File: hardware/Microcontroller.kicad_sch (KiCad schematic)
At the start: 1 part

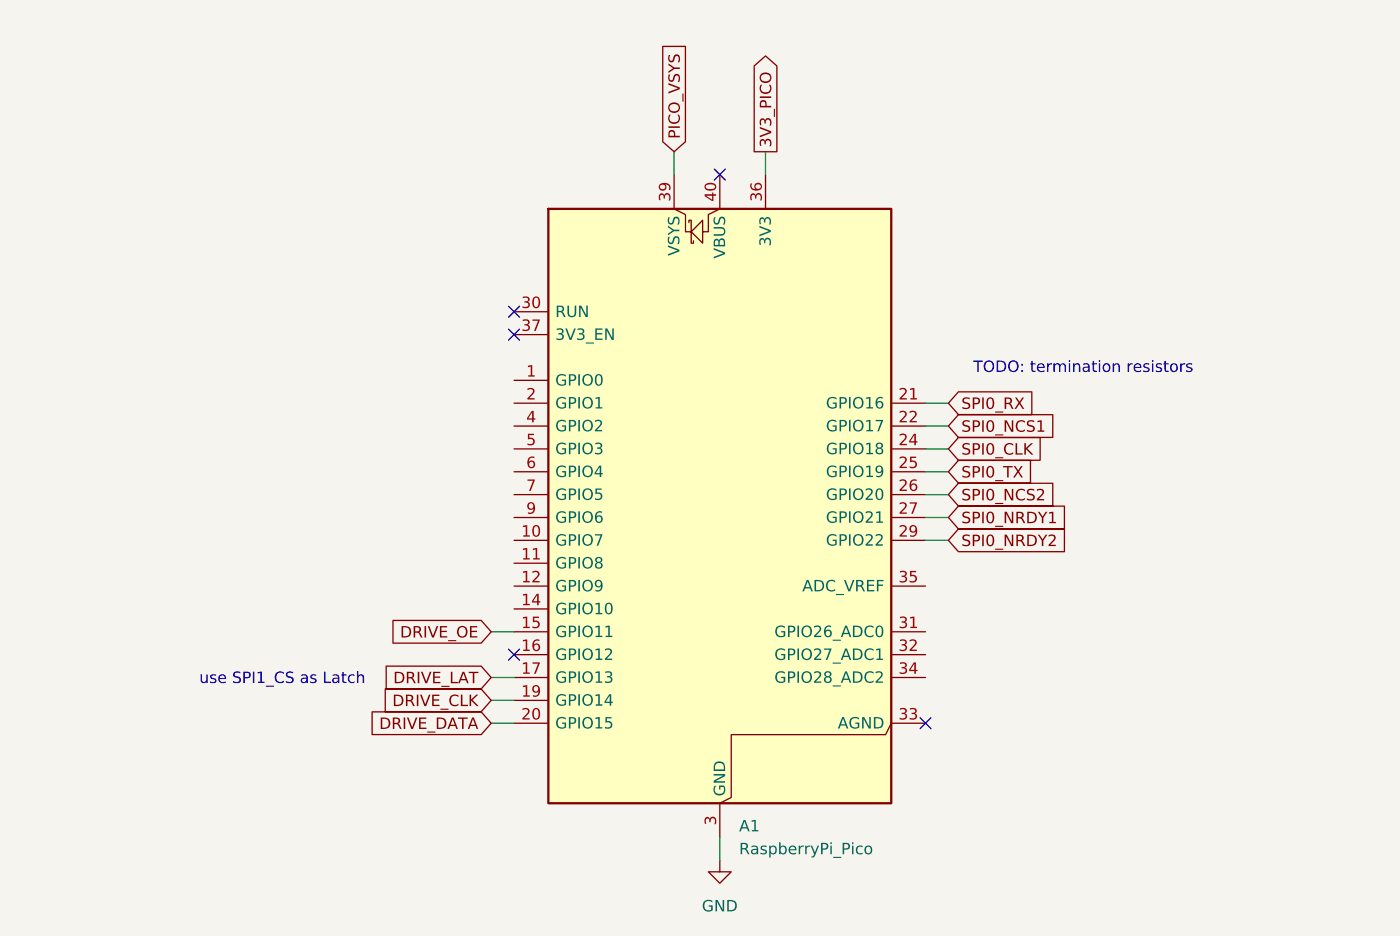
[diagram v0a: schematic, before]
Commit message: updated Power input on schematic
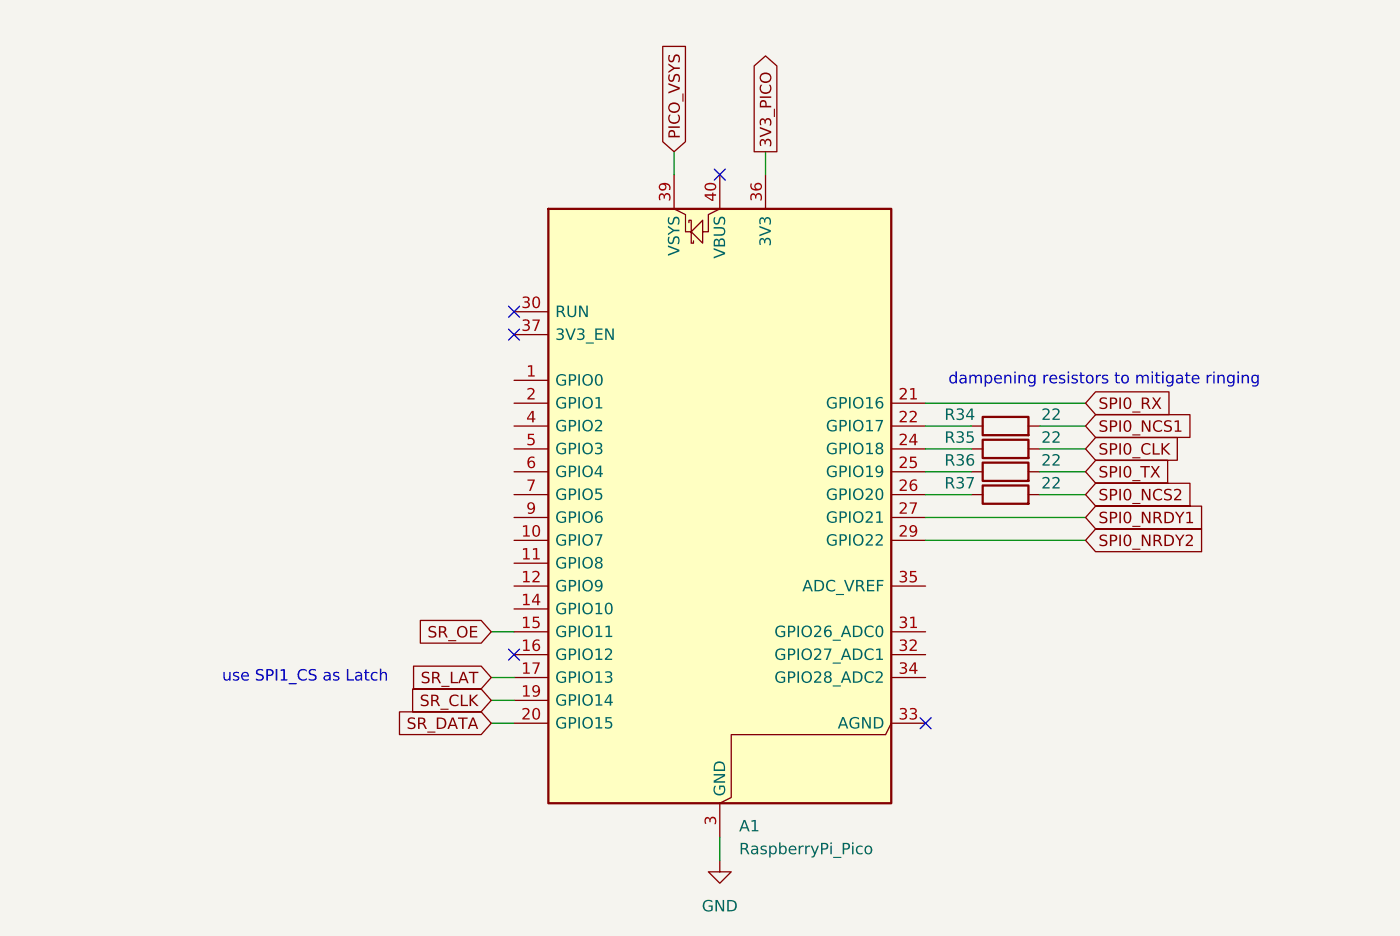
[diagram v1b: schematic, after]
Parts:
- added R34, R35, R36, R37: 22, symbol Device:R
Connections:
- net SPI0_CLK: now also R35.2; no longer A1.24 (GPIO18)
- net SPI0_NCS1: now also R34.2; no longer A1.22 (GPIO17)
- net SPI0_NCS2: now also R37.2; no longer A1.26 (GPIO20)
- net SPI0_TX: now also R36.2; no longer A1.25 (GPIO19)
- net DRIVE_CLK renamed SR_CLK
- net DRIVE_DATA renamed SR_DATA
- net DRIVE_LAT renamed SR_LAT
- net DRIVE_OE renamed SR_OE
- new net: A1.25 (GPIO19), R36.1
- new net: A1.24 (GPIO18), R35.1
- new net: A1.26 (GPIO20), R37.1
- new net: A1.22 (GPIO17), R34.1
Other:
- note added: "dampening resistors to mitigate ringing"
- note removed: "TODO: termination resistors"

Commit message: reworked power protection circuit and fixed ERC errors
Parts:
- R3: renamed from R34; footprint (none) -> Resistor_SMD:R_0603_1608Metric
- R4: renamed from R35; footprint (none) -> Resistor_SMD:R_0603_1608Metric
- R5: renamed from R36; footprint (none) -> Resistor_SMD:R_0603_1608Metric
- R6: renamed from R37; footprint (none) -> Resistor_SMD:R_0603_1608Metric
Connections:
- net LED_DI: now reaches A1.9 (GPIO6)
- no-connect marks 5 -> 19
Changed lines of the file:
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@@
+	)
+	(no_connect
+		(at 124.46 111.76)
+	)
+	(no_connect
+		(at 170.18 114.3)
 	)
 	(no_connect
@@
 	)
 	(no_connect
+		(at 170.18 119.38)
+	)
+	(no_connect
+		(at 124.46 109.22)
+	)
+	(no_connect
+		(at 124.46 96.52)
+	)
+	(no_connect
+		(at 124.46 116.84)
+	)
+	(no_connect
+		(at 124.46 93.98)
+	)
+	(no_connect
+		(at 124.46 99.06)
+	)
+	(no_connect
+		(at 170.18 124.46)
+	)
+	(no_connect
 		(at 170.18 129.54)
 	)
 	(no_connect
+		(at 124.46 91.44)
+	)
+	(no_connect
 		(at 124.46 121.92)
 	)
 	(no_connect
+		(at 124.46 101.6)
+	)
+	(no_connect
+		(at 124.46 114.3)
+	)
+	(no_connect
+		(at 170.18 121.92)
+	)
+	(no_connect
+		(at 124.46 104.14)
+	)
+	(no_connect
 		(at 124.46 86.36)
 	)
@@
 	(wire
 		(pts
+			(xy 152.4 66.04) (xy 152.4 68.58)
+		)
+		(stroke
+			(width 0)
+			(type default)
+		)
+	)
+	(wire
+		(pts
+			(xy 170.18 96.52) (xy 175.26 96.52)
+		)
+		(stroke
+			(width 0)
+			(type default)
+		)
+	)
+	(wire
+		(pts
+			(xy 121.92 124.46) (xy 124.46 124.46)
+		)
+		(stroke
+			(width 0)
+			(type default)
+		)
+	)
+	(wire
+		(pts
+			(xy 121.92 129.54) (xy 124.46 129.54)
+		)
+		(stroke
+			(width 0)
+			(type default)
+		)
+	)
+	(wire
+		(pts
+			(xy 182.88 96.52) (xy 187.96 96.52)
+		)
+		(stroke
+			(width 0)
+			(type default)
+		)
+	)
+	(wire
+		(pts
+			(xy 121.92 127) (xy 124.46 127)
+		)
+		(stroke
+			(width 0)
+			(type default)
+		)
+	)
+	(wire
+		(pts
+			(xy 170.18 106.68) (xy 187.96 106.68)
+		)
+		(stroke
+			(width 0)
+			(type default)
+		)
+	)
+	(wire
+		(pts
 			(xy 142.24 66.04) (xy 142.24 68.58)
 		)
@@
 	(wire
 		(pts
-			(xy 152.4 66.04) (xy 152.4 68.58)
-		)
-		(stroke
-			(width 0)
-			(type default)
-		)
-	)
-	(wire
-		(pts
-			(xy 170.18 96.52) (xy 175.26 96.52)
-		)
-		(stroke
-			(width 0)
-			(type default)
-		)
-	)
-	(wire
-		(pts
-			(xy 121.92 124.46) (xy 124.46 124.46)
-		)
-		(stroke
-			(width 0)
-			(type default)
-		)
-	)
-	(wire
-		(pts
-			(xy 121.92 129.54) (xy 124.46 129.54)
-		)
-		(stroke
-			(width 0)
-			(type default)
-		)
-	)
-	(wire
-		(pts
-			(xy 182.88 96.52) (xy 187.96 96.52)
-		)
-		(stroke
-			(width 0)
-			(type default)
-		)
-	)
-	(wire
-		(pts
-			(xy 121.92 127) (xy 124.46 127)
-		)
-		(stroke
-			(width 0)
-			(type default)
-		)
-	)
-	(wire
-		(pts
-			(xy 170.18 106.68) (xy 187.96 106.68)
+			(xy 121.92 106.68) (xy 124.46 106.68)
 		)
 		(stroke
@@
 		)
 	)
+	(global_label "LED_DI"
+		(shape input)
+		(at 121.92 106.68 180)
+		(fields_autoplaced yes)
+		(effects
+			(font
+				(size 1.27 1.27)
+			)
+			(justify right)
+		)
+		(property "Intersheetrefs" "${INTERSHEET_REFS}"
+			(at 112.6453 106.68 0)
+			(hide yes)
+			(show_name no)
+			(do_not_autoplace no)
+			(effects
+				(font
+					(size 1.27 1.27)
+				)
+				(justify right)
+			)
+		)
+	)
 	(global_label "SPI0_NRDY2"
 		(shape input)
@@
 		)
 	)
+	(global_label "PICO_VSYS"
+		(shape input)
+		(at 142.24 66.04 90)
+		(fields_autoplaced yes)
+		(effects
+			(font
+				(size 1.27 1.27)
+			)
+			(justify left)
+		)
+		(property "Intersheetrefs" "${INTERSHEET_REFS}"
+			(at 142.24 53.0157 90)
+			(hide yes)
+			(show_name no)
+			(do_not_autoplace no)
+			(effects
+				(font
+					(size 1.27 1.27)
+				)
+				(justify left)
+			)
+		)
+	)
 	(global_label "SR_DATA"
 		(shape input)
@@
 		)
 	)
-	(global_label "PICO_VSYS"
-		(shape input)
-		(at 142.24 66.04 90)
-		(fields_autoplaced yes)
-		(effects
-			(font
-				(size 1.27 1.27)
-			)
-			(justify left)
-		)
-		(property "Intersheetrefs" "${INTERSHEET_REFS}"
-			(at 142.24 53.0157 90)
-			(hide yes)
-			(show_name no)
-			(do_not_autoplace no)
-			(effects
-				(font
-					(size 1.27 1.27)
-				)
-				(justify left)
-			)
-		)
-	)
 	(global_label "3V3_PICO"
-		(shape output)
+		(shape input)
 		(at 152.4 66.04 90)
 		(fields_autoplaced yes)
@@
 		(in_pos_files yes)
 		(dnp no)
-		(property "Reference" "R36"
+		(property "Reference" "R5"
 			(at 173.99 100.33 90)
 			(show_name no)
@@
 			)
 		)
-		(property "Footprint" ""
+		(property "Footprint" "Resistor_SMD:R_0603_1608Metric"
 			(at 179.07 103.378 90)
 			(hide yes)
@@
 			(project "ExpressionController"
 				(path "/acb9d00b-1122-4203-9813-1d558ab77d86/6aaa6853-9d8e-4732-9d59-0d7219d4a5ec"
-					(reference "R36")
+					(reference "R5")
 					(unit 1)
 				)
@@
 		(in_pos_files yes)
 		(dnp no)
-		(property "Reference" "R35"
+		(property "Reference" "R4"
 			(at 173.99 97.79 90)
 			(show_name no)
@@
 			)
 		)
-		(property "Footprint" ""
+		(property "Footprint" "Resistor_SMD:R_0603_1608Metric"
 			(at 179.07 100.838 90)
 			(hide yes)
@@
 			(project "ExpressionController"
 				(path "/acb9d00b-1122-4203-9813-1d558ab77d86/6aaa6853-9d8e-4732-9d59-0d7219d4a5ec"
-					(reference "R35")
+					(reference "R4")
 					(unit 1)
 				)
@@
 		(in_pos_files yes)
 		(dnp no)
-		(property "Reference" "R37"
+		(property "Reference" "R6"
 			(at 173.99 102.87 90)
 			(show_name no)
@@
 			)
 		)
-		(property "Footprint" ""
+		(property "Footprint" "Resistor_SMD:R_0603_1608Metric"
 			(at 179.07 105.918 90)
 			(hide yes)
@@
 			(project "ExpressionController"
 				(path "/acb9d00b-1122-4203-9813-1d558ab77d86/6aaa6853-9d8e-4732-9d59-0d7219d4a5ec"
-					(reference "R37")
+					(reference "R6")
 					(unit 1)
 				)
@@
 		(dnp no)
 		(fields_autoplaced yes)
-		(property "Reference" "#PWR012"
+		(property "Reference" "#PWR01"
 			(at 147.32 151.13 0)
 			(hide yes)
@@
 			(project "ExpressionController"
 				(path "/acb9d00b-1122-4203-9813-1d558ab77d86/6aaa6853-9d8e-4732-9d59-0d7219d4a5ec"
-					(reference "#PWR012")
+					(reference "#PWR01")
 					(unit 1)
 				)
@@
 		(in_pos_files yes)
 		(dnp no)
-		(property "Reference" "R34"
+		(property "Reference" "R3"
 			(at 173.99 95.25 90)
 			(show_name no)
@@
 			)
 		)
-		(property "Footprint" ""
+		(property "Footprint" "Resistor_SMD:R_0603_1608Metric"
 			(at 179.07 98.298 90)
 			(hide yes)
@@
 			(project "ExpressionController"
 				(path "/acb9d00b-1122-4203-9813-1d558ab77d86/6aaa6853-9d8e-4732-9d59-0d7219d4a5ec"
-					(reference "R34")
+					(reference "R3")
 					(unit 1)
 				)

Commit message: added basic PCB ordering
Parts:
- added R46, R47, R48, R49: 22, Resistor_SMD:R_0603_1608Metric, symbol Device:R
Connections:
- net SR_CLK: now also R48.1; no longer A1.19 (GPIO14)
- net SR_DATA: now also R49.1; no longer A1.20 (GPIO15)
- net SR_LAT: now also R47.1; no longer A1.17 (GPIO13)
- net SR_OE: now also R46.1; no longer A1.15 (GPIO11)
- new net: A1.15 (GPIO11), R46.2
- new net: A1.17 (GPIO13), R47.2
- new net: A1.19 (GPIO14), R48.2
- new net: A1.20 (GPIO15), R49.2

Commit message: added all footprints, updated to 0805, added layout for Jacks
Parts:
- R3, R4, R46, R47, R48, R49, R5, R6: footprint Resistor_SMD:R_0603_1608Metric -> Resistor_SMD:R_0805_2012Metric
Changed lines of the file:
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@@
 			)
 		)
-		(property "Footprint" "Resistor_SMD:R_0603_1608Metric"
+		(property "Footprint" "Resistor_SMD:R_0805_2012Metric"
 			(at 179.07 103.378 90)
 			(hide yes)
@@
 			)
 		)
-		(property "Footprint" "Resistor_SMD:R_0603_1608Metric"
+		(property "Footprint" "Resistor_SMD:R_0805_2012Metric"
 			(at 115.57 121.158 90)
 			(hide yes)
@@
 			)
 		)
-		(property "Footprint" "Resistor_SMD:R_0603_1608Metric"
+		(property "Footprint" "Resistor_SMD:R_0805_2012Metric"
 			(at 179.07 100.838 90)
 			(hide yes)
@@
 			)
 		)
-		(property "Footprint" "Resistor_SMD:R_0603_1608Metric"
+		(property "Footprint" "Resistor_SMD:R_0805_2012Metric"
 			(at 179.07 105.918 90)
 			(hide yes)
@@
 			)
 		)
-		(property "Footprint" "Resistor_SMD:R_0603_1608Metric"
+		(property "Footprint" "Resistor_SMD:R_0805_2012Metric"
 			(at 179.07 98.298 90)
 			(hide yes)
@@
 			)
 		)
-		(property "Footprint" "Resistor_SMD:R_0603_1608Metric"
+		(property "Footprint" "Resistor_SMD:R_0805_2012Metric"
 			(at 115.57 126.238 90)
 			(hide yes)
@@
 			)
 		)
-		(property "Footprint" "Resistor_SMD:R_0603_1608Metric"
+		(property "Footprint" "Resistor_SMD:R_0805_2012Metric"
 			(at 115.57 131.318 90)
 			(hide yes)
@@
 			)
 		)
-		(property "Footprint" "Resistor_SMD:R_0603_1608Metric"
+		(property "Footprint" "Resistor_SMD:R_0805_2012Metric"
 			(at 115.57 128.778 90)
 			(hide yes)

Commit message: more progress in layout
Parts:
- A1: footprint Module:RaspberryPi_Pico_Common_Unspecified -> Pico_2W_with_Header:Pico_2W_with_Header
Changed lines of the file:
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@@
 			)
 		)
-		(property "Footprint" "Module:RaspberryPi_Pico_Common_Unspecified"
+		(property "Footprint" "Pico_2W_with_Header:Pico_2W_with_Header"
 			(at 147.32 153.67 0)
 			(hide yes)

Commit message: replaced buffer ICs with analog switches, schematic bugfixes, started new routing
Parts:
- added R58: 10k, Resistor_SMD:R_0805_2012Metric, symbol Device:R
- R3, R4, R46, R47, R48, R49, R5, R6: value 22 -> 47
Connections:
- net SR_OE: now also R58.1
- net SR_WB: now reaches A1.16 (GPIO12)
- net 3V3_PICO: no longer names the net of A1.36 (3V3)
- new net +3.3VA: R58.2
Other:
- note removed: "dampening resistors to mitigate ringing"
- note removed: "use SPI1_CS as Latch"

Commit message: added mouser part numbers
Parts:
- A1, R3, R4, R46, R47, R48, R49, R5, R58, R6: Part Source (none) -> Uni

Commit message: more routing progress
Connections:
- net SR_OE: no longer R58.1
- net at A1.15 (GPIO11), R46.2: now also R58.1
- net SR_WB: no longer names the net of A1.16 (GPIO12)
- no-connect marks 19 -> 20
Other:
- moved on the sheet: R46, R47, R48, R49
